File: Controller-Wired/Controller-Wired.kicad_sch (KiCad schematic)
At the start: 7 parts, among them J1 Conn_02x20_Odd_Even, U1 STM32F103CBTx

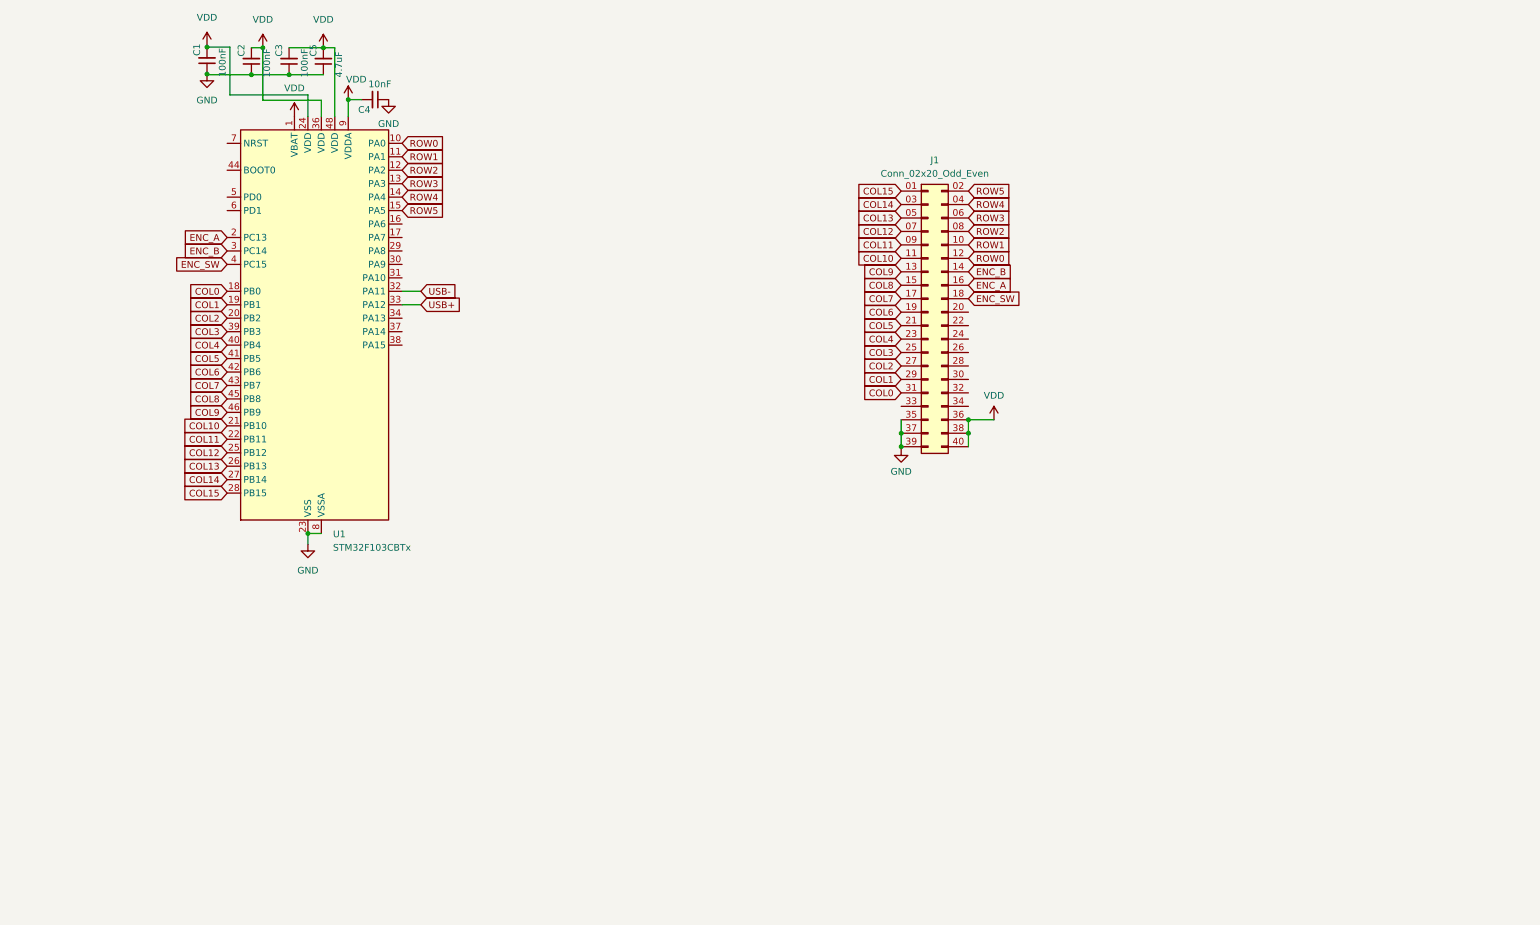
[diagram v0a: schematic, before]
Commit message: Started Controller Routing
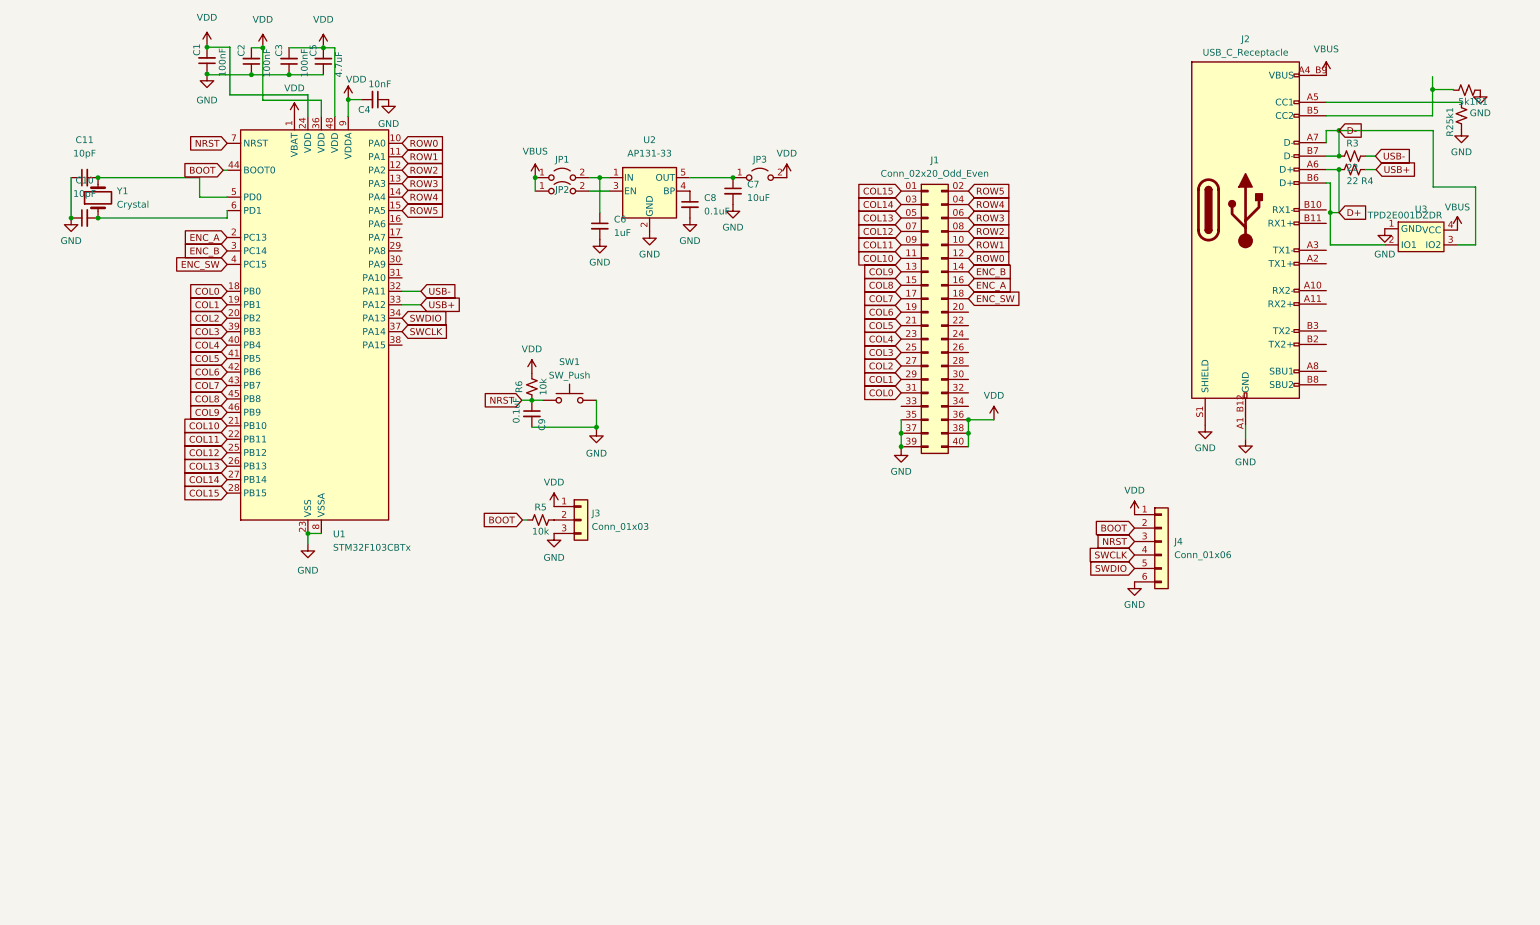
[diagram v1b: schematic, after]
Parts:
- added C10, C11: 10pF, Capacitor_SMD:C_0805_2012Metric_Pad1.18x1.45mm_HandSolder, symbol Device:C_Small
- added C6: 1uF, Capacitor_SMD:C_0805_2012Metric_Pad1.18x1.45mm_HandSolder, symbol Device:C_Small
- added C7: 10uF, Capacitor_SMD:C_0805_2012Metric_Pad1.18x1.45mm_HandSolder, symbol Device:C_Small
- added C8, C9: 0.1uF, Capacitor_SMD:C_0805_2012Metric_Pad1.18x1.45mm_HandSolder, symbol Device:C_Small
- added J2: USB_C_Receptacle, Controller:AMPHENOL_12402012E212A, symbol Connector:USB_C_Receptacle
- added J3: Conn_01x03, Connector_PinHeader_2.54mm:PinHeader_1x03_P2.54mm_Vertical, symbol Connector_Generic:Conn_01x03
- added J4: Conn_01x06, Connector_PinHeader_2.54mm:PinHeader_1x06_P2.54mm_Vertical, symbol Connector_Generic:Conn_01x06
- added JP1, JP2, JP3: Jumper_2_Open, Connector_PinHeader_2.54mm:PinHeader_1x02_P2.54mm_Vertical, symbol Jumper:Jumper_2_Open
- added R1, R2: 5k1, Resistor_SMD:R_0805_2012Metric_Pad1.20x1.40mm_HandSolder, symbol Device:R_Small_US
- added R3, R4: 22, Resistor_SMD:R_0805_2012Metric_Pad1.20x1.40mm_HandSolder, symbol Device:R_Small_US
- added R5, R6: 10k, Resistor_SMD:R_0805_2012Metric_Pad1.20x1.40mm_HandSolder, symbol Device:R_Small_US
- added SW1: SW_Push, Button_Switch_SMD:SW_SPST_B3SL-1002P, symbol Switch:SW_Push
- added U2: AP131-33, Package_TO_SOT_SMD:SOT-23-5, symbol Regulator_Linear:AP131-33
- added U3: TPD2E001DZDR, Controller:SOT192P237X122-4N, symbol Keyboard:TPD20E001DZDR
- added Y1: Crystal, Controller:XTAL_ABM3-8.000MHZ-D2Y-T_ABR, symbol Device:Crystal
- J1: DigikeyPN (none) -> SAM13720TR-ND
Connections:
- net GND: now also C10.1, C11.1, C6.2, C7.2, C8.2, C9.2, J2.A1_B12 (GND), J2.B1_A12 (GND), J2.S1 (SHIELD), J3.3 (Pin_3), J4.6 (Pin_6), R1.2, R2.2, SW1.2, U2.2 (GND), U3.1 (GND)
- net USB+: now also R4.2
- net USB-: now also R3.2
- net VDD: now also J3.1 (Pin_1), J4.1 (Pin_1), JP3.2 (B), R6.2
- net SWDIO: now reaches U1.34 (PA13)
- net SWDIO: now also J4.5 (Pin_5)
- net SWCLK: now reaches U1.37 (PA14)
- net SWCLK: now also J4.4 (Pin_4)
- net BOOT: now reaches U1.44 (BOOT0)
- net BOOT: now also J4.2 (Pin_2), R5.1
- net at U1.5 (PD0): now also C11.2, Y1.2
- net at U1.6 (PD1): now also C10.2, Y1.1
- net NRST: now reaches U1.7 (NRST)
- net NRST: now also C9.1, J4.3 (Pin_3), R6.1, SW1.1
- new net: J2.A5 (CC1), R2.1
- new net: J2.B5 (CC2), R1.1
- new net: C7.1, JP3.1 (A), U2.5 (OUT)
- new net: J3.2 (Pin_2), R5.2
- new net: JP2.2 (B), U2.3 (EN)
- new net: C6.1, JP1.2 (B), U2.1 (IN)
- new net: C8.1, U2.4 (BP)
- new net D+: J2.A6 (D+), J2.B6 (D+), R4.1, U3.2 (IO1)
- new net D-: J2.A7 (D-), J2.B7 (D-), R3.1, U3.3 (IO2)
- new net VBUS: J2.A4_B9 (VBUS), J2.B4_A9 (VBUS), JP1.1 (A), JP2.1 (A), U3.4 (VCC)

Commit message: Reworking the layout, and changed the ESD Protection
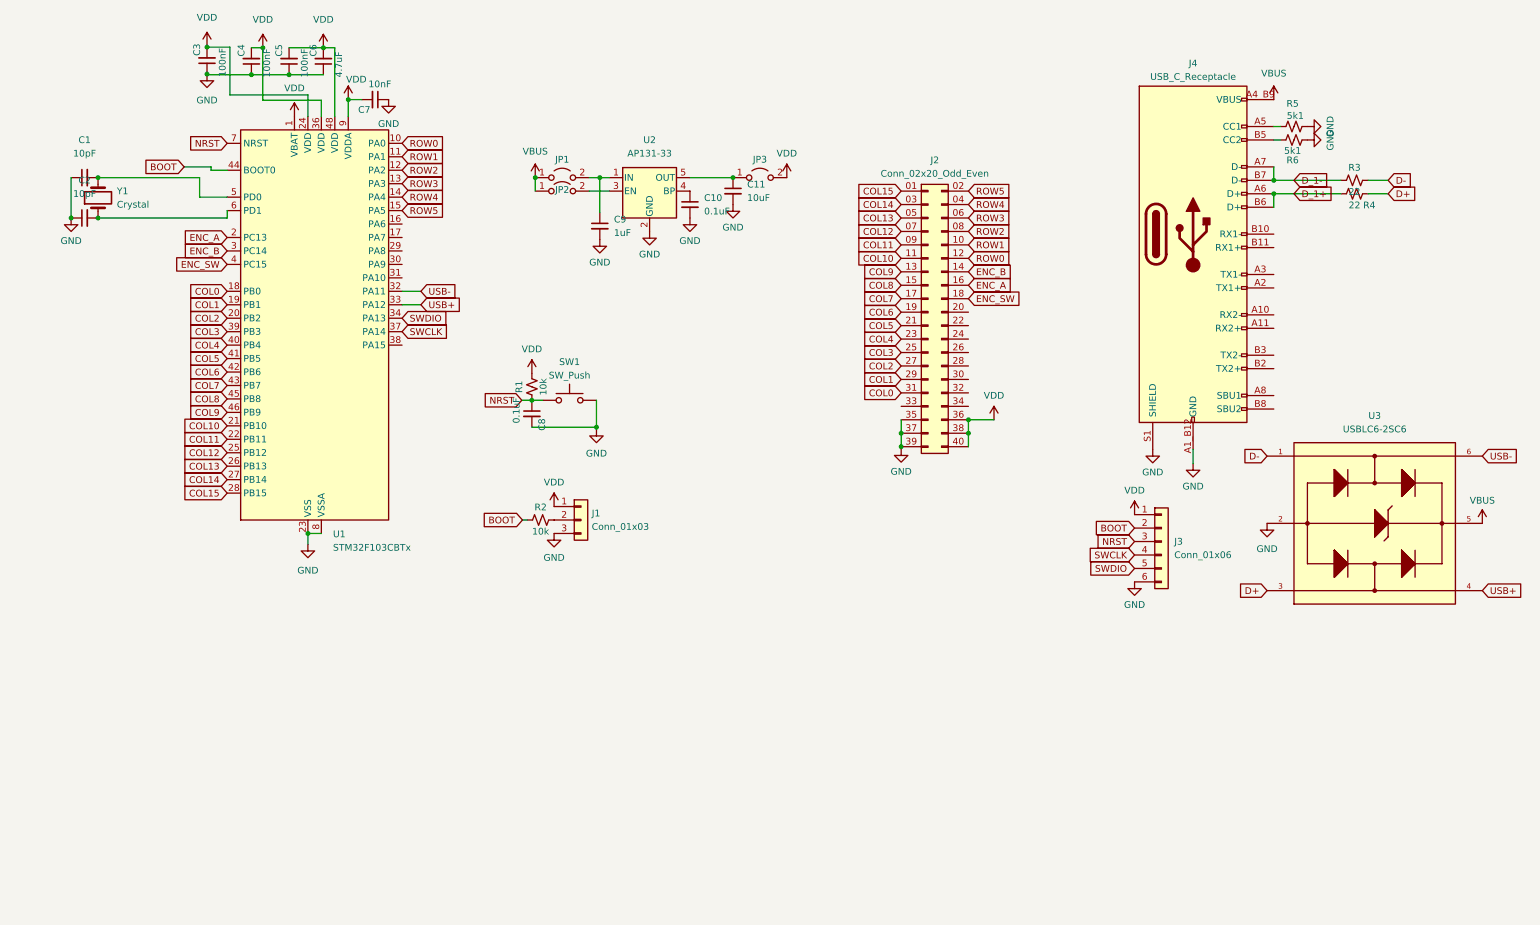
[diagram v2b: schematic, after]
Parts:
- removed U3: TPD2E001DZDR, Controller:SOT192P237X122-4N, symbol Keyboard:TPD20E001DZDR
- added U3: USBLC6-2SC6, Controller:SOT95P280X145-6N, symbol Keyboard:USBLC6-2SC6
- renumbered C11 to C1, C8 to C10, C7 to C11, C10 to C2, C1 to C3, C2 to C4, C3 to C5, C5 to C6, C4 to C7, C9 to C8, C6 to C9, J3 to J1, J1 to J2, J4 to J3, J2 to J4, R6 to R1, R5 to R2, R2 to R5, R1 to R6
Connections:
- net D+: now also R4.2, U3.3; no longer J4.A6 (D+), J4.B6 (D+), R4.1
- net D-: now also R3.2, U3.1; no longer J4.A7 (D-), J4.B7 (D-), R3.1
- net GND: now also R6.1, U3.2; no longer R6.2
- net USB+: now also U3.4; no longer R4.2
- net USB-: now also U3.6; no longer R3.2
- net VBUS: now also U3.5
- net at J4.B5 (CC2): now also R6.2; no longer R6.1
- new net D_1+: J4.A6 (D+), J4.B6 (D+), R4.1
- new net D_1-: J4.A7 (D-), J4.B7 (D-), R3.1
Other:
- moved on the sheet: J4, R3, R4, R5, R6

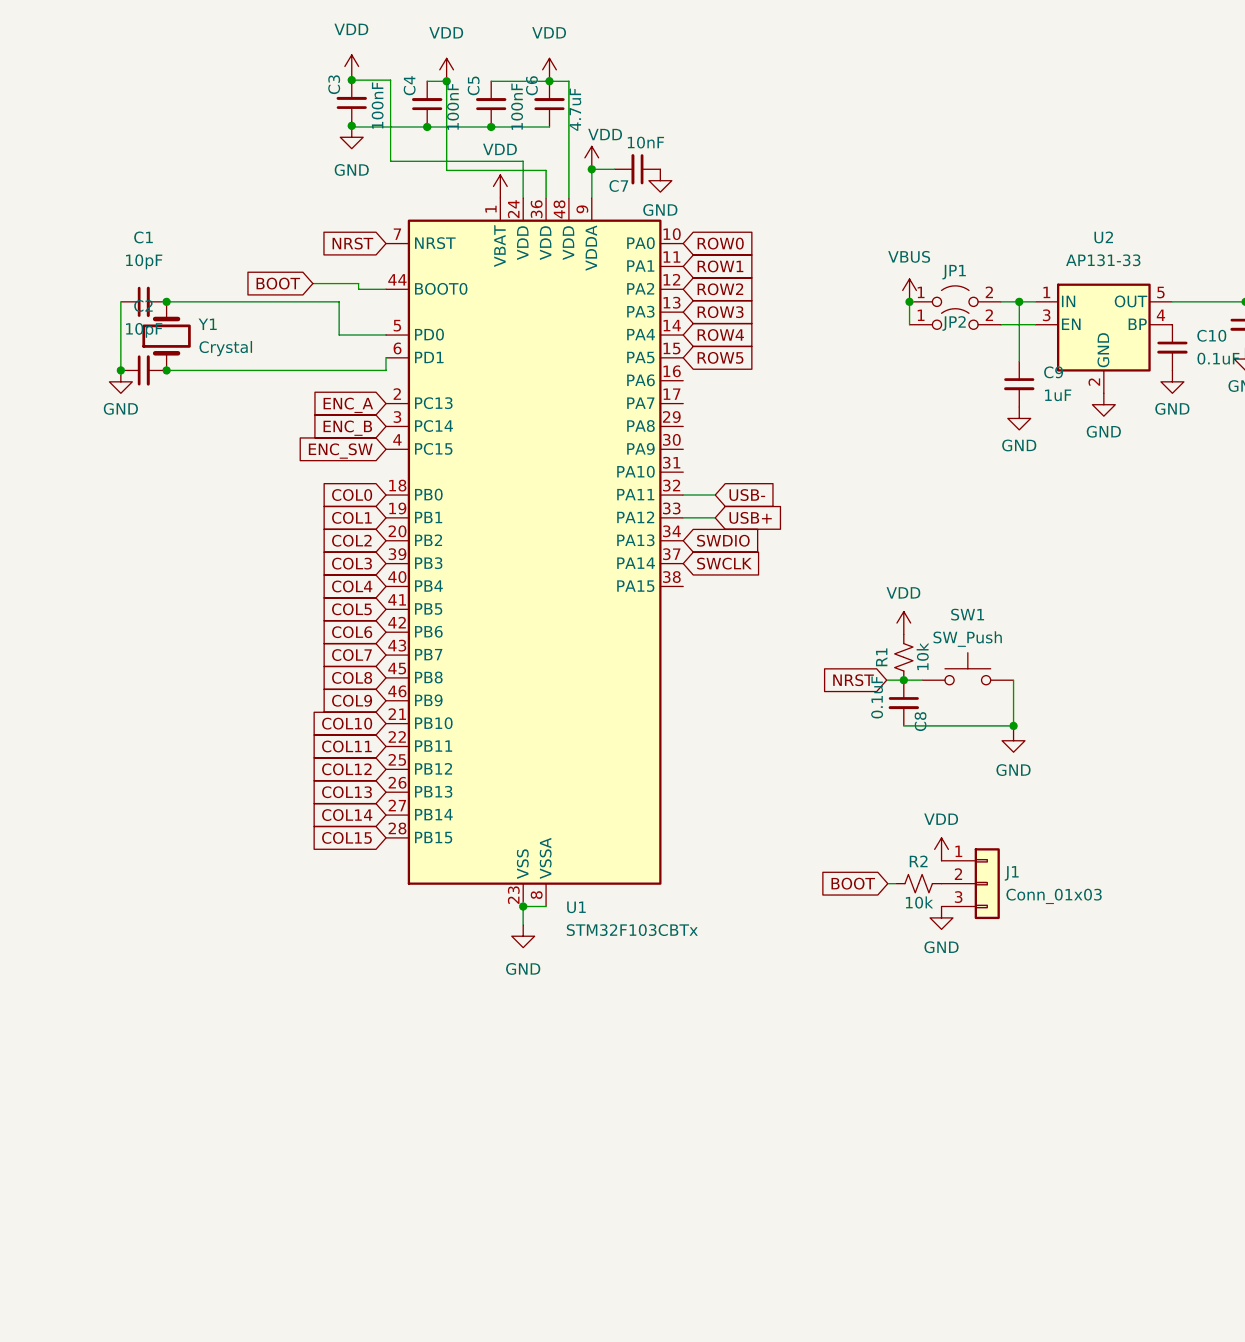
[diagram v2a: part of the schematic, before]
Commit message: Finished First Rev Of Both PCB's, after testing fits in freecad, will  move onto ordrering board
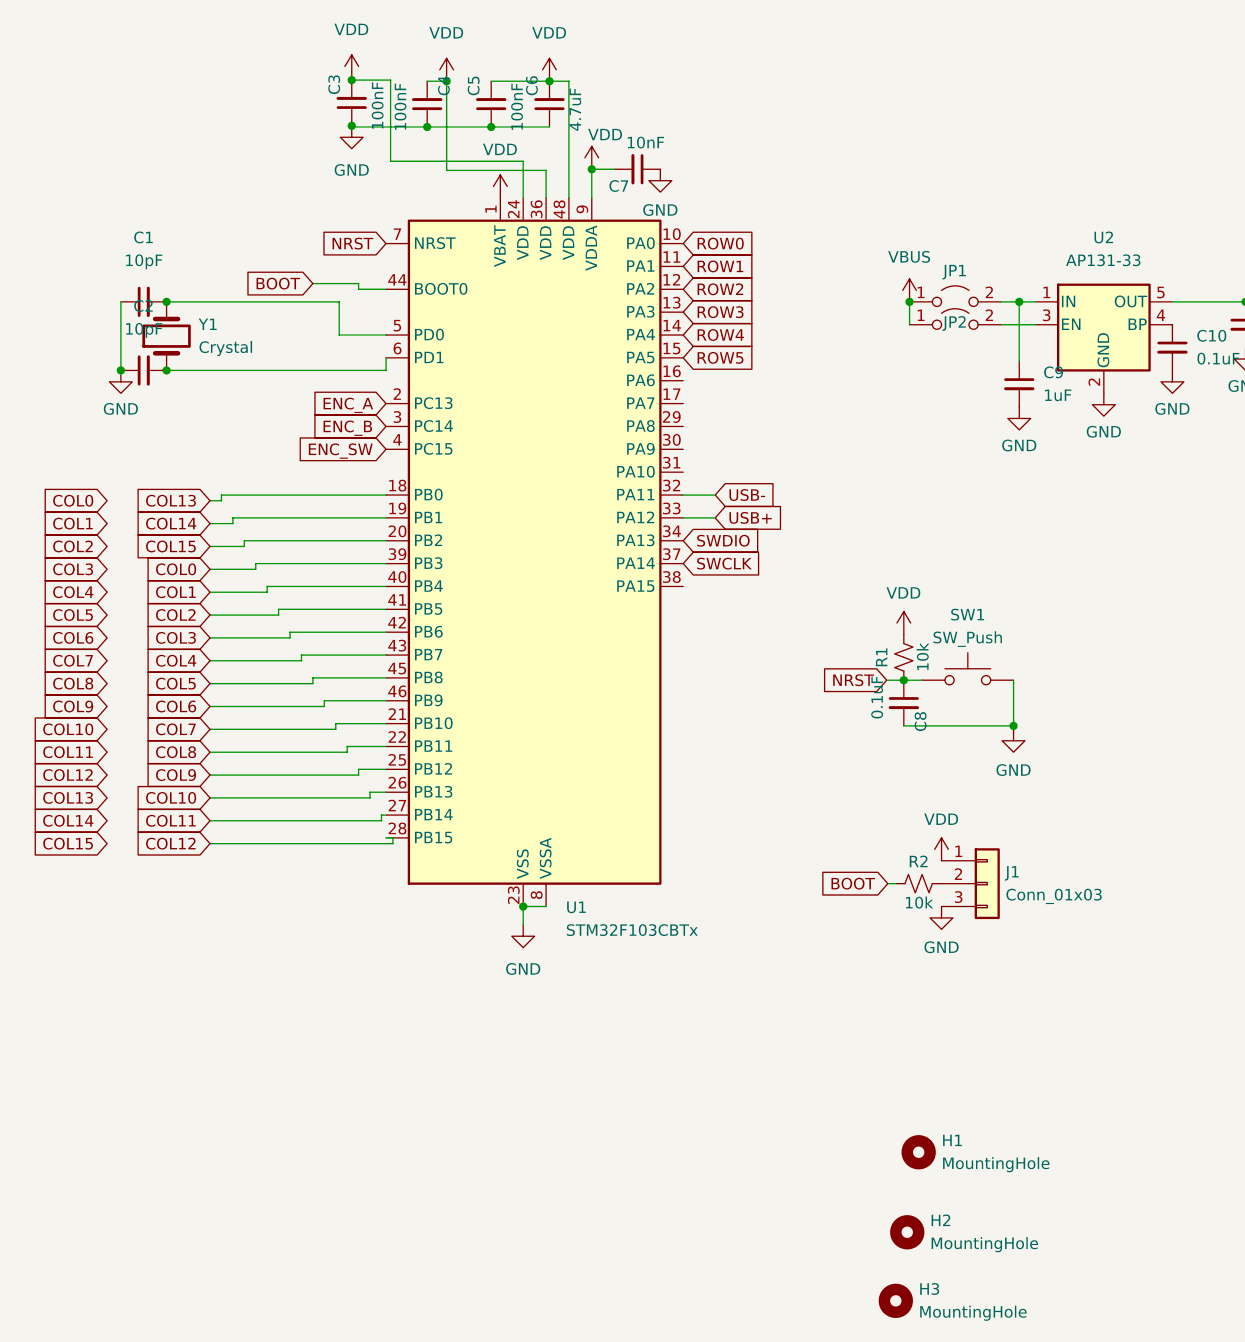
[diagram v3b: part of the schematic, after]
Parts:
- added H1, H2, H3: MountingHole, MountingHole:MountingHole_3.2mm_M3_Pad_Via, symbol Mechanical:MountingHole
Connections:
- net COL0: now also U1.39 (PB3); no longer U1.18 (PB0)
- net COL1: now also U1.40 (PB4); no longer U1.19 (PB1)
- net COL10: now also U1.26 (PB13); no longer U1.21 (PB10)
- net COL11: now also U1.27 (PB14); no longer U1.22 (PB11)
- net COL12: now also U1.28 (PB15); no longer U1.25 (PB12)
- net COL13: now also U1.18 (PB0); no longer U1.26 (PB13)
- net COL14: now also U1.19 (PB1); no longer U1.27 (PB14)
- net COL15: now also U1.20 (PB2); no longer U1.28 (PB15)
- net COL2: now also U1.41 (PB5); no longer U1.20 (PB2)
- net COL3: now also U1.42 (PB6); no longer U1.39 (PB3)
- net COL4: now also U1.43 (PB7); no longer U1.40 (PB4)
- net COL5: now also U1.45 (PB8); no longer U1.41 (PB5)
- net COL6: now also U1.46 (PB9); no longer U1.42 (PB6)
- net COL7: now also U1.21 (PB10); no longer U1.43 (PB7)
- net COL8: now also U1.22 (PB11); no longer U1.45 (PB8)
- net COL9: now also U1.25 (PB12); no longer U1.46 (PB9)
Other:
- moved on the sheet: C4
